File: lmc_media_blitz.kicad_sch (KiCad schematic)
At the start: 57 parts, among them J3 Conn_01x12, J4 Conn_01x12, J5 Conn_ARM_JTAG_SWD_10, Q1 BSS138W, Q2 BSS138W, SW1 SW_Push, SW2 SW_Push, SW3 SW_Push, U1 XC6206PxxxMR, U2 TPS613222ADBV, U3 STM32F030C8Tx

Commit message: Added I2C resistors to schematic, cleaned up unused parts and started layout
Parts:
- removed C16: 22nF, Capacitor_SMD:C_0805_2012Metric, symbol Device:C
- removed J5: Conn_ARM_JTAG_SWD_10, Connector_PinHeader_1.27mm:PinHeader_2x05_P1.27mm_Vertical_SMD, symbol Connector:Conn_ARM_JTAG_SWD_10
- removed R10, R11: 10K, Resistor_SMD:R_0805_2012Metric, symbol Device:R
- added R1, R2: 4k7, Resistor_SMD:R_0805_2012Metric, symbol Device:R
- TP10, TP4, TP5, TP6, TP7, TP8, TP9: footprint TestPoint:TestPoint_Pad_D2.0mm -> TestPoint:TestPoint_Pad_D1.5mm
- renumbered R8 to R10, R9 to R11, R1 to R4, R2 to R5, R4 to R6, R5 to R7, R6 to R8, R7 to R9, SW2 to SW1, SW1 to SW2
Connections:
- net +3V3: now also R1.1, R2.1
- net I2C1_SCL: now also R2.2
- net I2C1_SDA: now also R1.2
- net SWCLK: now also J4.2 (Pin_2); no longer J4.3 (Pin_3)
- net nRST: now also J4.3 (Pin_3); no longer J4.2 (Pin_2)
- no-connect marks 21 -> 20
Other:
- removed sheet NFC

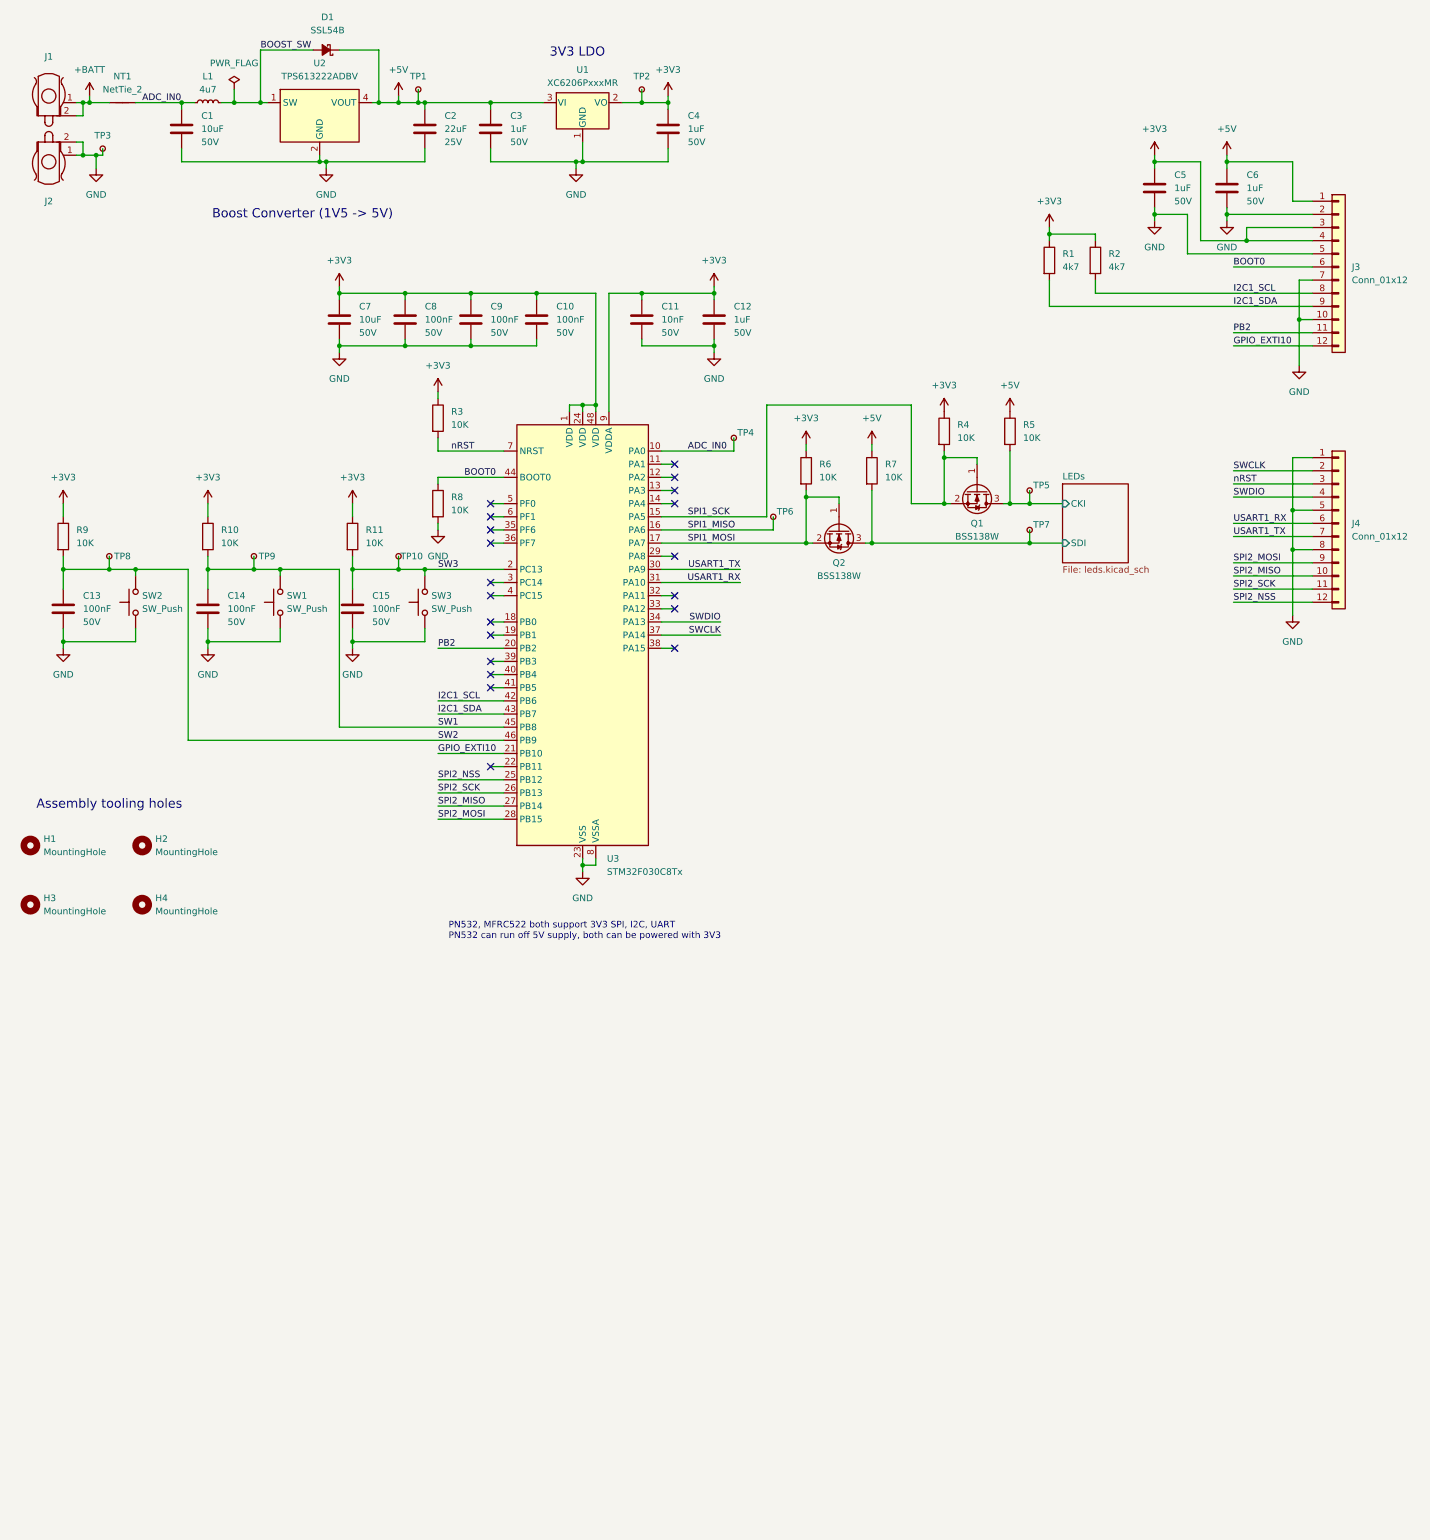
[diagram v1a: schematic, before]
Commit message: Updated MCU and connector pinout to make routing more convenient.  Power circuit still to be routed
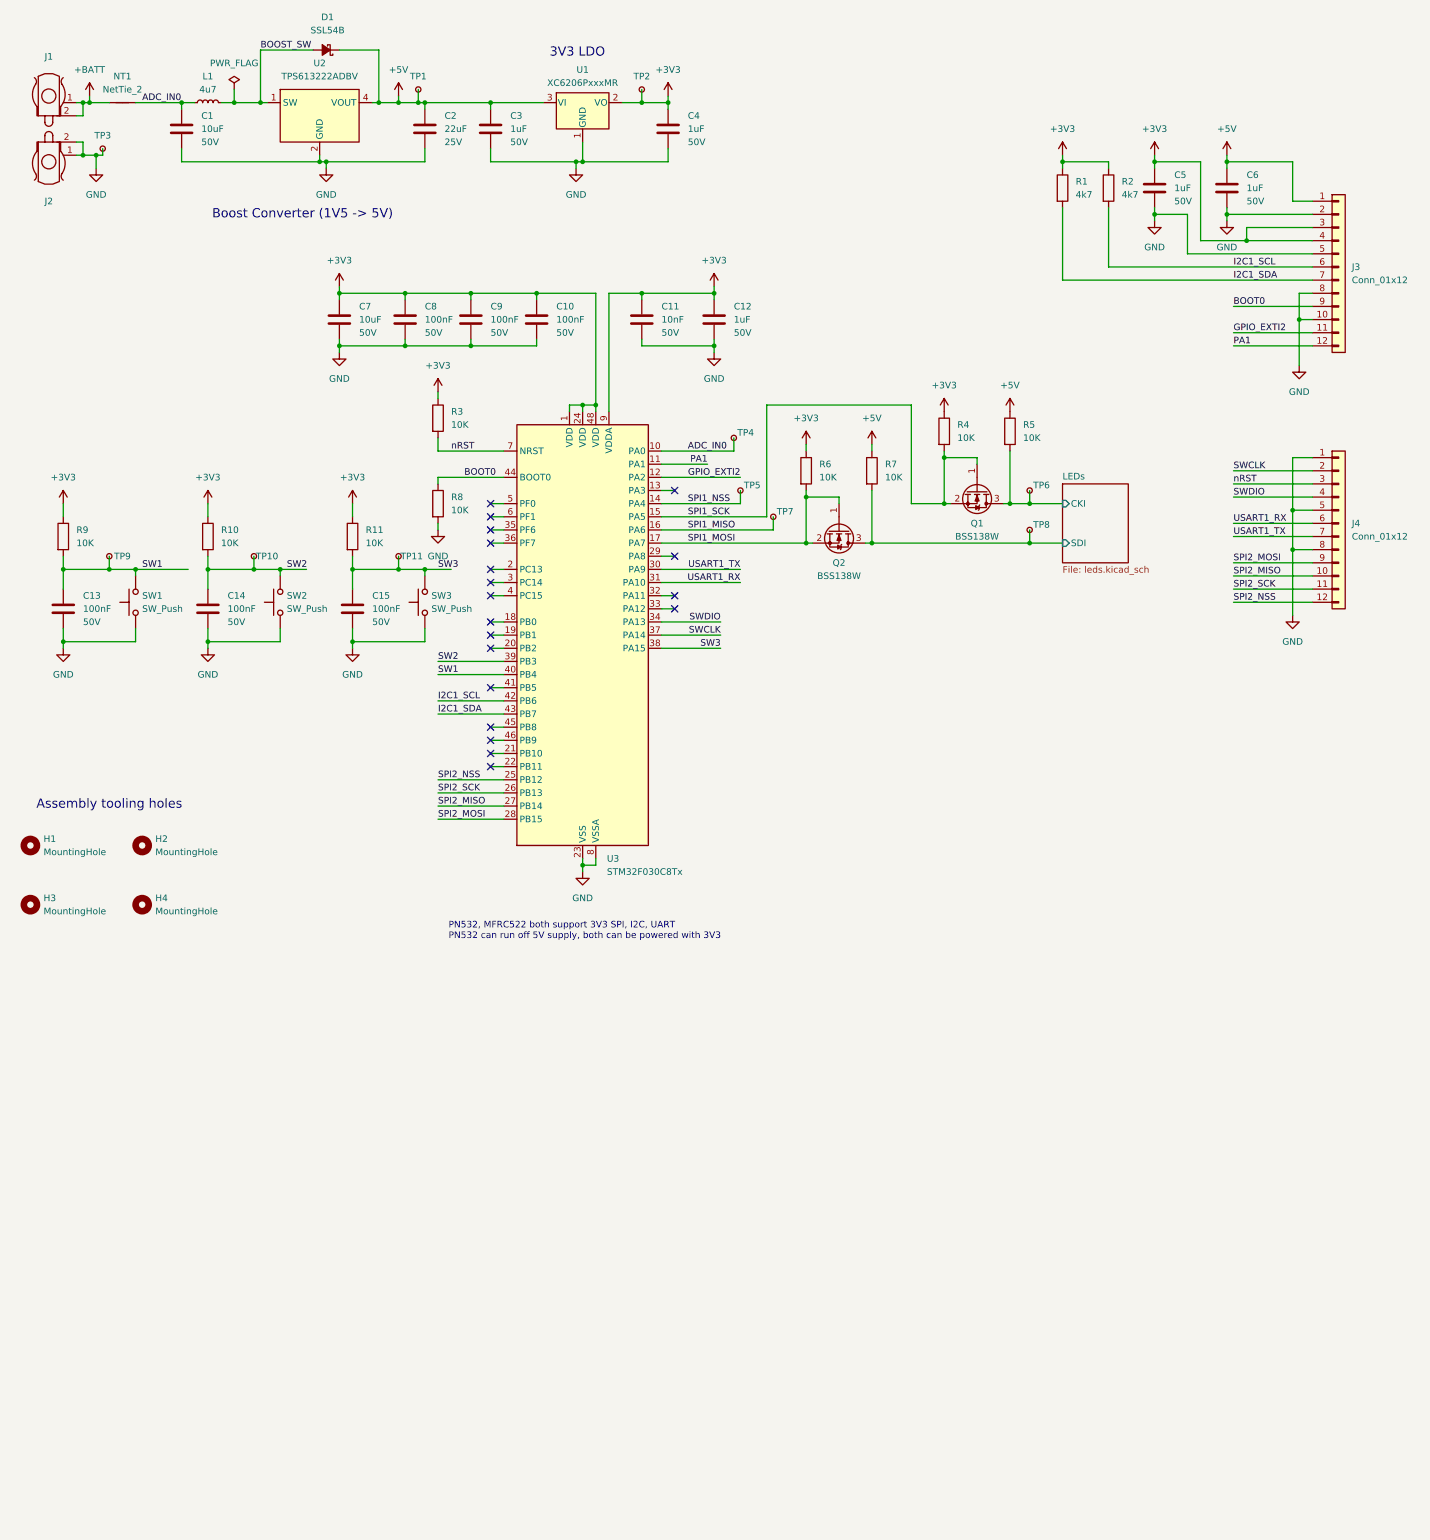
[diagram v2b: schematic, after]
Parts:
- added TP5: TestPoint_Small, TestPoint:TestPoint_Pad_D1.5mm, symbol Connector:TestPoint_Small
- renumbered SW2 to SW1, SW1 to SW2, TP9 to TP10, TP10 to TP11, TP5 to TP6, TP6 to TP7, TP7 to TP8, TP8 to TP9
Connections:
- net BOOT0: now also J3.9 (Pin_9); no longer J3.6 (Pin_6)
- net GND: now also J3.8 (Pin_8); no longer J3.7 (Pin_7)
- net I2C1_SCL: now also J3.6 (Pin_6); no longer J3.8 (Pin_8)
- net I2C1_SDA: now also J3.7 (Pin_7); no longer J3.9 (Pin_9)
- net SW1: now also C13.1, R9.2, SW1.2, TP9.1, U3.40 (PB4); no longer C14.1, R10.2, SW2.2, TP10.1, U3.45 (PB8)
- net SW2: now also C14.1, R10.2, SW2.2, TP10.1, U3.39 (PB3); no longer C13.1, R9.2, SW1.2, TP9.1, U3.46 (PB9)
- net SW3: now also U3.38 (PA15); no longer U3.2 (PC13)
- net PA1: now reaches U3.11 (PA1)
- net PA1: now also J3.12 (Pin_12)
- net GPIO_EXTI2: now reaches U3.12 (PA2)
- net GPIO_EXTI2: now also J3.11 (Pin_11)
- net SPI1_NSS: now reaches U3.14 (PA4)
- net SPI1_NSS: now also TP5.1
- net GPIO_EXTI10: no longer names the net of U3.21 (PB10)
- net GPIO_EXTI10: no longer J3.12 (Pin_12)
- net PB2: no longer names the net of U3.20 (PB2)
- net PB2: no longer J3.11 (Pin_11)
- no-connect marks 20 -> 19
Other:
- moved on the sheet: R1, R2

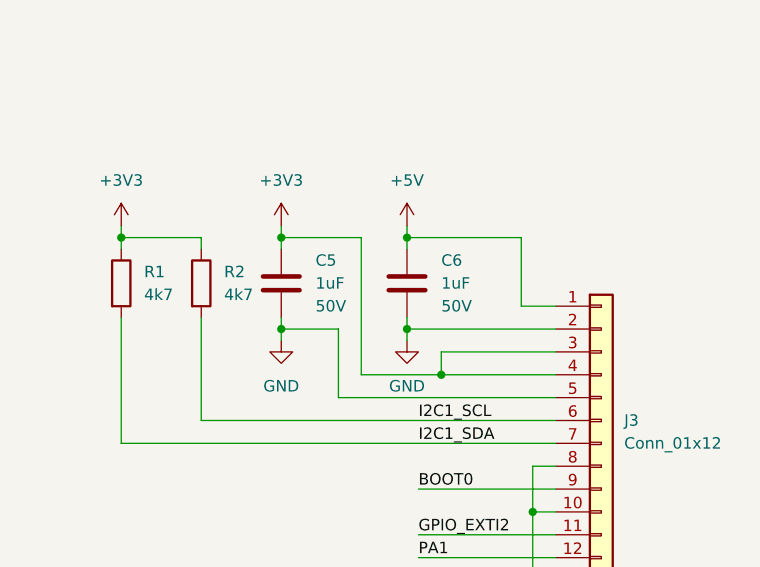
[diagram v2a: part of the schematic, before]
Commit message: Changed board shape to be narrow around the pin headers to fit on a breadboard.  Still not sufficiently narrow
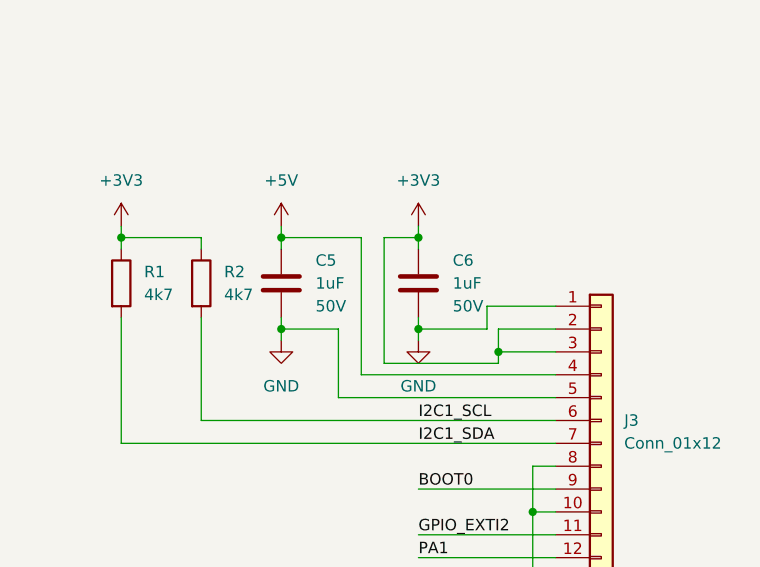
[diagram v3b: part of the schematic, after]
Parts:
- TP1, TP2, TP3: footprint TestPoint:TestPoint_Pad_D2.0mm -> TestPoint:TestPoint_Pad_D1.5mm
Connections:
- net +3V3: now also C6.1, J3.2 (Pin_2); no longer C5.1, J3.4 (Pin_4)
- net +5V: now also C5.1, J3.4 (Pin_4); no longer C6.1, J3.1 (Pin_1)
- net GND: now also J3.1 (Pin_1); no longer J3.2 (Pin_2)
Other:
- moved on the sheet: C6
